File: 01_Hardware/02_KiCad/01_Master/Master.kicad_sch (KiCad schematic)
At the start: 8 parts, among them J1 Conn_01x30_Female, J2 Conn_01x30_Female, Q1 BS170, U1 INA180A1

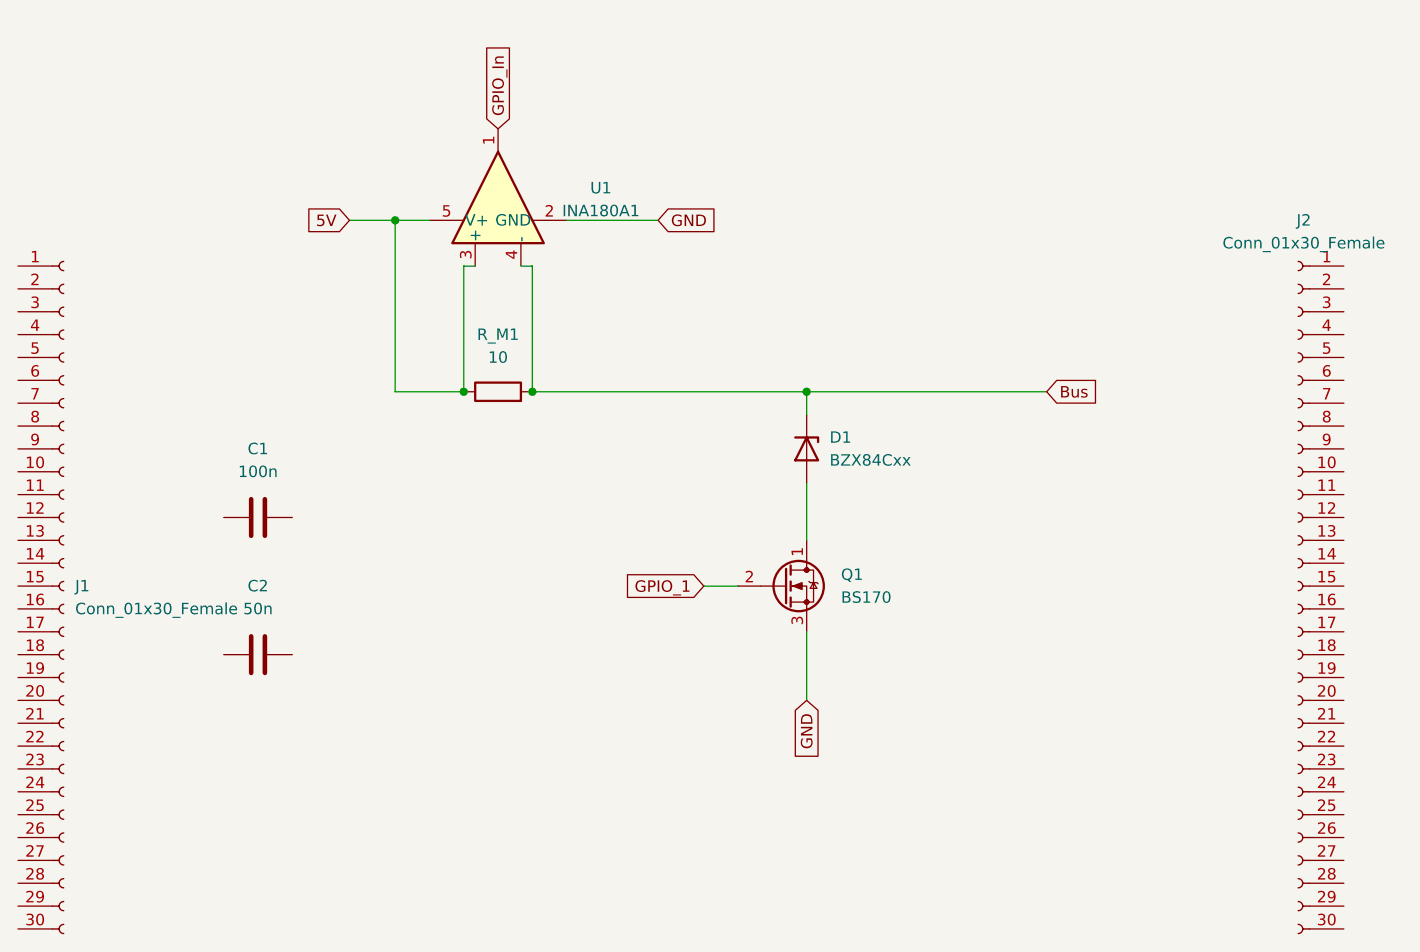
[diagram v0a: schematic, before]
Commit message: Master and Slave Prototyp finsished! JLCPCB ordered
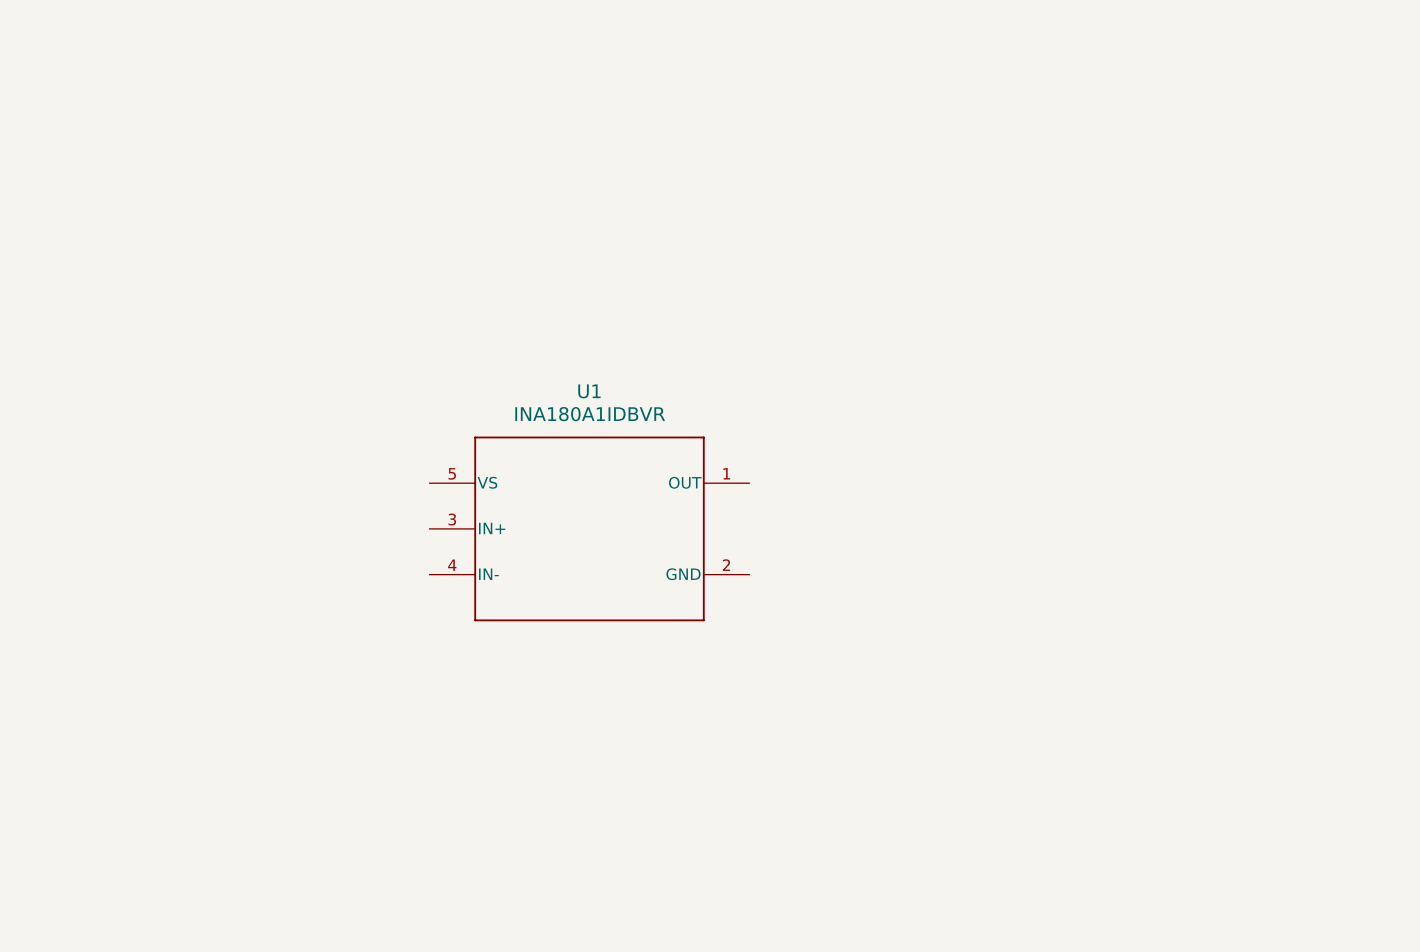
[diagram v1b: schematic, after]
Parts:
- removed C1: 100n, Capacitor_THT:C_Axial_L3.8mm_D2.6mm_P7.50mm_Horizontal, symbol Device:C
- removed C2: 50n, Capacitor_THT:C_Axial_L3.8mm_D2.6mm_P7.50mm_Horizontal, symbol Device:C
- removed D1: BZX84Cxx, Package_TO_SOT_SMD:SOT-23, symbol Diode:BZX84Cxx
- removed J1, J2: Conn_01x30_Female, Connector_PinSocket_2.54mm:PinSocket_1x30_P2.54mm_Vertical, symbol Connector:Conn_01x30_Female
- removed Q1: BS170, Package_TO_SOT_THT:TO-92_Inline_Horizontal1, symbol Transistor_FET:BS170
- removed R_M1: 10, Resistor_THT:R_Axial_DIN0204_L3.6mm_D1.6mm_P5.08mm_Horizontal, symbol Device:R
- removed U1: INA180A1, Package_TO_SOT_SMD:SOT-23-5, symbol Amplifier_Current:INA180A1
- added U1: INA180A1IDBVR, DBV0005A_N, symbol INA180A1IDBVR:INA180A1IDBVR
